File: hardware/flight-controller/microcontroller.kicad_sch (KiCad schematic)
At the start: 32 parts, among them J2 Conn_01x05, SW2 SW_Push, U4 ESP-12E, U5 STM32U535RET6, Y1 8MHz

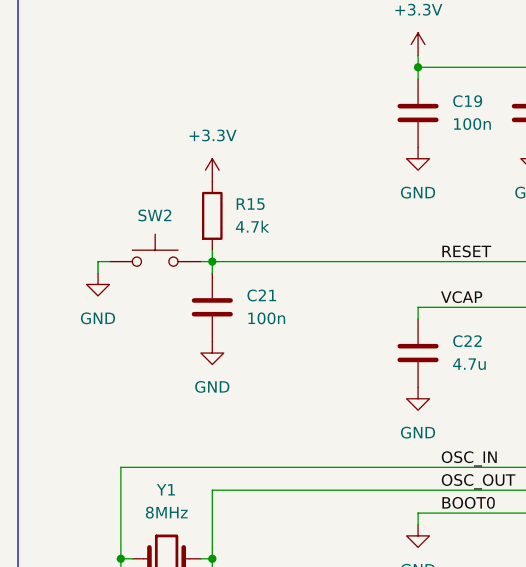
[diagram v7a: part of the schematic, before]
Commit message: switches footprints
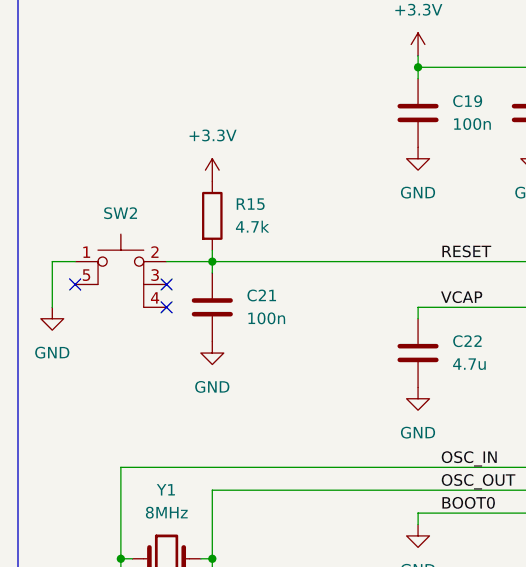
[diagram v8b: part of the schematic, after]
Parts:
- removed SW2: SW_Push, symbol Switch:SW_Push
- added SW2: ~, goose:KMS231GPLFS, symbol goose:SW5
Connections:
- net GND: now also SW2.1
- net RESET: now also SW2.2
- no-connect marks 20 -> 23
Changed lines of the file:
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@@
 	)
 	(no_connect
+		(at 36.83 93.98)
+	)
+	(no_connect
 		(at 245.11 87.63)
 	)
 	(no_connect
+		(at 36.83 91.44)
+	)
+	(no_connect
 		(at 214.63 82.55)
 	)
@@
 	)
 	(no_connect
+		(at 26.67 91.44)
+	)
+	(no_connect
 		(at 214.63 77.47)
 	)
@@
 	(wire
 		(pts
-			(xy 29.21 88.9) (xy 30.48 88.9)
+			(xy 24.13 88.9) (xy 26.67 88.9)
 		)
 		(stroke
@@
 	(wire
 		(pts
-			(xy 40.64 88.9) (xy 41.91 88.9)
+			(xy 256.54 67.31) (xy 265.43 67.31)
 		)
 		(stroke
@@
 	(wire
 		(pts
-			(xy 256.54 67.31) (xy 265.43 67.31)
+			(xy 92.71 82.55) (xy 92.71 81.28)
 		)
 		(stroke
@@
 	(wire
 		(pts
-			(xy 92.71 82.55) (xy 92.71 81.28)
+			(xy 36.83 88.9) (xy 41.91 88.9)
 		)
 		(stroke
@@
 	(wire
 		(pts
-			(xy 29.21 90.17) (xy 29.21 88.9)
+			(xy 24.13 93.98) (xy 24.13 88.9)
 		)
 		(stroke
@@
 	(symbol
 		(lib_id "power:GND")
-		(at 29.21 90.17 0)
+		(at 24.13 93.98 0)
 		(unit 1)
 		(exclude_from_sim no)
@@
 		(fields_autoplaced yes)
 		(property "Reference" "#PWR040"
-			(at 29.21 96.52 0)
+			(at 24.13 100.33 0)
 			(effects
 				(font
@@
 		)
 		(property "Value" "GND"
-			(at 29.21 95.25 0)
+			(at 24.13 99.06 0)
 			(effects
 				(font
@@
 		)
 		(property "Footprint" ""
-			(at 29.21 90.17 0)
+			(at 24.13 93.98 0)
 			(effects
 				(font
@@
 		)
 		(property "Datasheet" ""
-			(at 29.21 90.17 0)
+			(at 24.13 93.98 0)
 			(effects
 				(font
@@
 		)
 		(property "Description" "Power symbol creates a global label with name \"GND\" , ground"
-			(at 29.21 90.17 0)
+			(at 24.13 93.98 0)
 			(effects
 				(font
@@
 	)
 	(symbol
+		(lib_id "goose:SW5")
+		(at 31.75 88.9 0)
+		(unit 1)
+		(exclude_from_sim no)
+		(in_bom yes)
+		(on_board yes)
+		(dnp no)
+		(property "Reference" "SW2"
+			(at 31.75 83.566 0)
+			(effects
+				(font
+					(size 1.27 1.27)
+				)
+			)
+		)
+		(property "Value" "~"
+			(at 31.75 83.82 0)
+			(effects
+				(font
+					(size 1.27 1.27)
+				)
+			)
+		)
+		(property "Footprint" "goose:KMS231GPLFS"
+			(at 31.75 83.82 0)
+			(effects
+				(font
+					(size 1.27 1.27)
+				)
+				(hide yes)
+			)
+		)
+		(property "Datasheet" ""
+			(at 31.75 83.82 0)
+			(effects
+				(font
+					(size 1.27 1.27)
+				)
+				(hide yes)
+			)
+		)
+		(property "Description" ""
+			(at 31.75 83.82 0)
+			(effects
+				(font
+					(size 1.27 1.27)
+				)
+				(hide yes)
+			)
+		)
+		(pin "1"
+		)
+		(pin "4"
+		)
+		(pin "5"
+		)
+		(pin "3"
+		)
+		(pin "2"
+		)
+		(instances
+			(project ""
+				(path "/52d2474d-2865-43c6-846b-d5f8a367c5f4/33ee6dd5-762c-4c0c-85b1-322db5527c00"
+					(reference "SW2")
+					(unit 1)
+				)
+			)
+		)
+	)
+	(symbol
 		(lib_id "Device:C")
 		(at 64.77 72.39 0)
@@
 					(unit 1)
 				)
-			)
-		)
-	)
-	(symbol
-		(lib_id "Switch:SW_Push")
-		(at 35.56 88.9 0)
-		(unit 1)
-		(exclude_from_sim no)
-		(in_bom yes)
-		(on_board yes)
-		(dnp no)
-		(fields_autoplaced yes)
-		(property "Reference" "SW2"
-			(at 35.56 83.82 0)
-			(effects
-				(font
-					(size 1.27 1.27)
-				)
-			)
-		)
-		(property "Value" "SW_Push"
-			(at 35.56 83.82 0)
-			(effects
-				(font
-					(size 1.27 1.27)
-				)
-				(hide yes)
-			)
-		)
-		(property "Footprint" ""
-			(at 35.56 83.82 0)
-			(effects
-				(font
-					(size 1.27 1.27)
-				)
-				(hide yes)
-			)
-		)
-		(property "Datasheet" "~"
-			(at 35.56 83.82 0)
-			(effects
-				(font
-					(size 1.27 1.27)
-				)
-				(hide yes)
-			)
-		)
-		(property "Description" "Push button switch, generic, two pins"
-			(at 35.56 88.9 0)
-			(effects
-				(font
-					(size 1.27 1.27)
-				)
-				(hide yes)
-			)
-		)
-		(pin "2"
-		)
-		(pin "1"
-		)
-		(instances
-			(project "flight-controller"
-				(path "/52d2474d-2865-43c6-846b-d5f8a367c5f4/33ee6dd5-762c-4c0c-85b1-322db5527c00"
-					(reference "SW2")
-					(unit 1)
-				)
